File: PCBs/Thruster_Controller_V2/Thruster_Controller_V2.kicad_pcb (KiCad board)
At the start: 4 copper layers, 35.5 x 37 mm, 112 parts, among them J1 PHASE_A, J2 PHASE_B, J3 PHASE_C, J4 Conn_01x01, J5 Pogo Conn, J6 Conn_01x01, J7 Conn_01x01, J8 Conn_01x01, Q1 SIZF906DT, Q2 SIZF906DT, Q3 SIZF906DT, U1 NCP718AMT330, U2 TMS320F280041C, U3 DRV8320S, U4 NCP718BMT500, U8 ATA6561, Y1 20 MHz

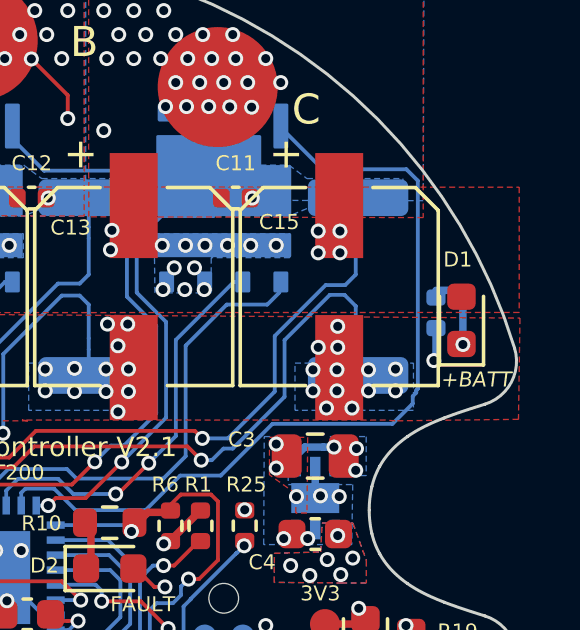
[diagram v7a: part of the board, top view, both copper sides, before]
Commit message: Fixed a woopsies
- Change R7 from 0402 to 0603 for future board spins
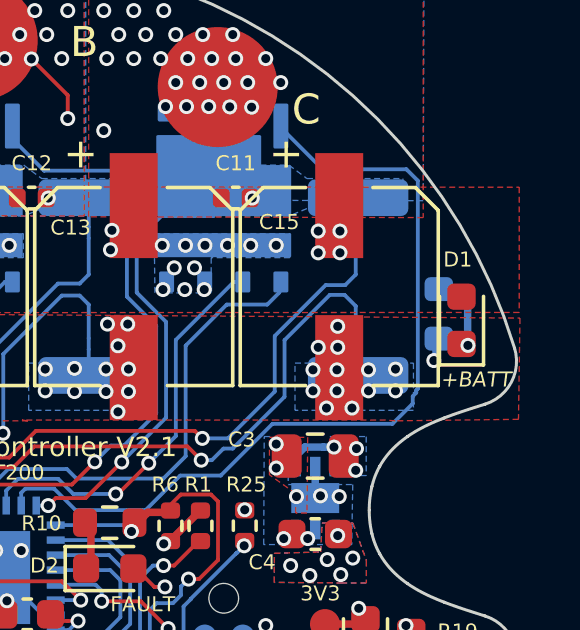
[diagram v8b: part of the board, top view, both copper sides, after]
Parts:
- R7: footprint Resistor_SMD:R_0402_1005Metric -> Resistor_SMD:R_0603_1608Metric
- U4: value NCP718BMT500 -> NCP718AMT500
- moved R7 0.10 mm to (115.2, 91.7)
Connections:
- J5 pad 10: (no net) -> /TRST
